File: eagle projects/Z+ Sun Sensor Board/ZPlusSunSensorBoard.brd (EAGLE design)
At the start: 78 x 78 mm, 53 parts, among them U2 ADS7841E_2K5, U4 LM20BIM7X_NOPB, U6 TLV9051IDCKR, U8 TLV9051IDCKR, U9 TLV9051IDCKR

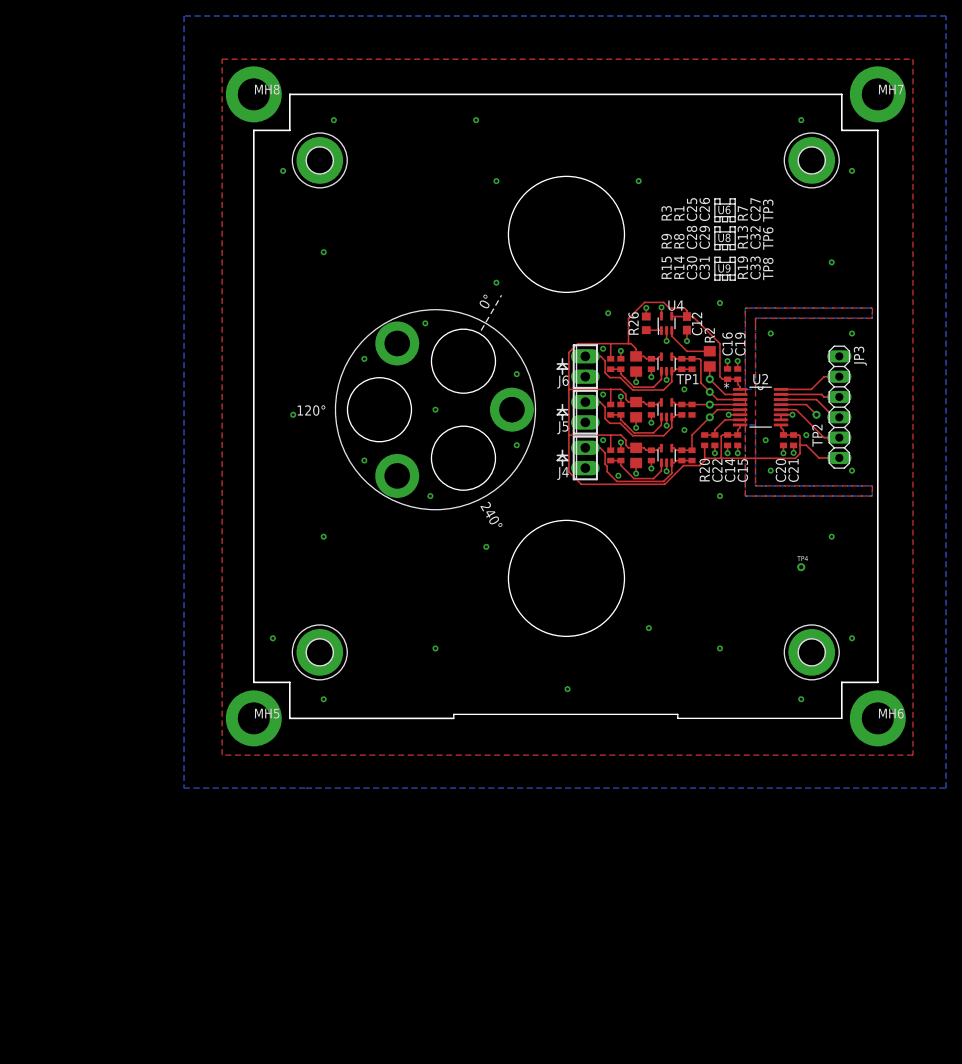
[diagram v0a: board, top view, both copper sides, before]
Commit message: updates to Z+ sun sense board for 3d models
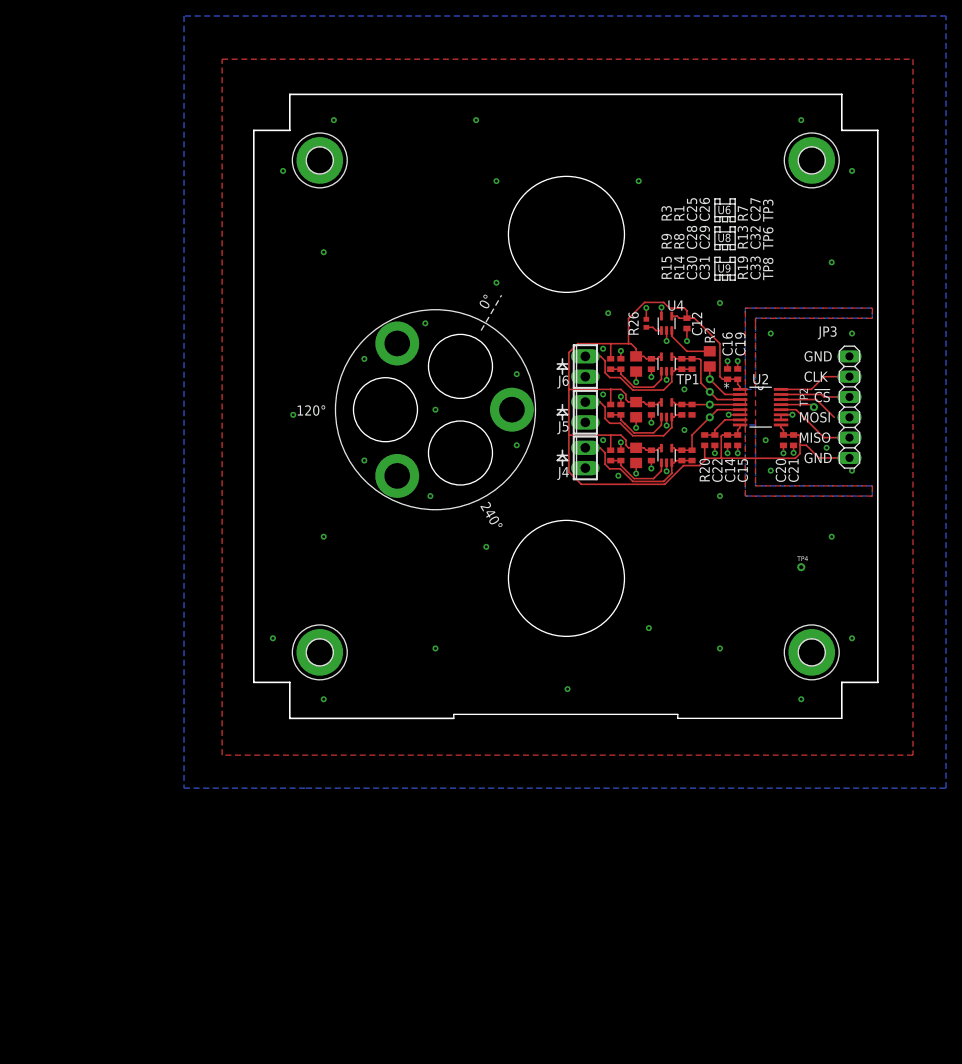
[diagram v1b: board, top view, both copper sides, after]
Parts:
- removed MH5, MH6, MH7, MH8: MTGP700H400, my_library:MTGP700H400
- C12: device rcl:C0603 -> rcl:C0402
- C27, C32, C33: value 0.015u -> 0.022u
- R13, R19, R7: value 5.6k -> 3.74k
- R26: device rcl:R0603 -> rcl:R0402
- moved JP3 1.27 mm to (81.0, 45.4)
- moved TP2 1.00 mm to (76.5, 45.4)
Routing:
- net +3V3: track 138.2 -> 139.8 mm
- net UCB0_SPI_MISO: track 8.74 -> 10.0 mm
- net UCB0_SPI_CLK: track 7.95 -> 9.22 mm
- net !CS!_SUN_Z+: track 7.42 -> 8.69 mm
- net N$2: track 4.96 -> 4.25 mm
- net GND: track 28.2 -> 28.8 mm
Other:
- board text added: "!CS"
- board text added: "CLK"
- board text added: "GND"
- board text added: "MISO"
- board text added: "MOSI"
- board text added: "Z+ SUN SENSE BOARD - Rev A"
- board text removed: "Z+ SUN SENSOR BOARD - Rev A"

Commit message: Finalized sun sense board
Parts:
- added DRILEGEND: (no value), drilegend:DRILEGEND
- H1, H2, H3, H4: value MOUNT-PAD-ROUND3.2 -> MOUNT-PAD-ROUND; device holes:3,2-PAD -> my_library:PC104
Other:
- outline, holes or cut-outs redrawn
- board text added: "+3V3"
- board text added: "01-16"
- board text added: "01-20"
- board text added: "LAYER-STACK"

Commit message: Minor gerber updates to copper
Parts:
- JP3: device pinhead:1X06 -> my_library:1X06
- moved R2 0.32 mm to (63.5, 51.8)
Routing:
- net GND: track 28.8 -> 26.7 mm, vias 69 -> 70
- net UCB0_SPI_MOSI: track 7.58 -> 9.48 mm
- net N$8: track 16.5 -> 17.8 mm

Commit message: bfwebfibc
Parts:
- added R4: 5.1M, resistor:R0402
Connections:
- net GND: now also R4.1
- net N$2: now also R4.2
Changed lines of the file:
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@@
 </element>
 <element name="DRILEGEND" library="drilegend" package="DRILEGEND" value="" x="-4.57708125" y="-7.75208125" smashed="yes"/>
+<element name="R4" library="resistor" library_urn="urn:adsk.eagle:library:348" package="R0402" package3d_urn="urn:adsk.eagle:package:26058/2" value="5.1M" x="-22.225" y="-34.29" smashed="yes">
+<attribute name="NAME" x="-22.86" y="-33.655" size="1.27" layer="25"/>
+<attribute name="VALUE" x="-22.86" y="-36.195" size="1.27" layer="27"/>
+</element>
 </elements>
 <signals>
@@
 </polygon>
 <via x="65.7225" y="43.18" extent="1-16" drill="0.35"/>
+<contactref element="R4" pad="1"/>
+<wire x1="74.93" y1="81.28" x2="81.28" y2="74.93" width="0" layer="19" extent="1-1"/>
+<wire x1="78.74" y1="63.5" x2="81.28" y2="74.93" width="0" layer="19" extent="1-1"/>
+<wire x1="81.28" y1="54.61" x2="78.74" y2="63.5" width="0" layer="19" extent="1-1"/>
+<wire x1="80.9625" y1="51.7525" x2="81.28" y2="54.61" width="0" layer="19" extent="1-1"/>
+<wire x1="71.12" y1="54.61" x2="81.28" y2="54.61" width="0" layer="19" extent="1-1"/>
+<wire x1="66.04" y1="55.88" x2="71.12" y2="54.61" width="0" layer="19" extent="1-1"/>
+<wire x1="65.7225" y1="51.1606" x2="66.04" y2="55.88" width="0" layer="19" extent="1-1"/>
+<wire x1="66.9925" y1="51.1606" x2="65.7225" y2="51.1606" width="0" layer="19" extent="1-1"/>
+<wire x1="60.6425" y1="55.23" x2="66.04" y2="55.88" width="0" layer="19" extent="1-1"/>
+<wire x1="58.1025" y1="53.665659375" x2="60.6425" y2="53.6575" width="0" layer="19" extent="1-1"/>
+<wire x1="57.4525" y1="56.78" x2="58.1025" y2="54.98" width="0" layer="19" extent="1-1"/>
+<wire x1="55.5625" y1="57.8106" x2="57.4675" y2="57.8656" width="0" layer="19" extent="1-1"/>
+<wire x1="58.1025" y1="49.89" x2="58.1025" y2="53.665659375" width="0" layer="19" extent="1-1"/>
+<wire x1="56.1975" y1="50.15" x2="58.1025" y2="49.89" width="0" layer="19" extent="1-1"/>
+<wire x1="54.2925" y1="49.85" x2="56.1975" y2="50.15" width="0" layer="19" extent="1-1"/>
+<wire x1="52.3875" y1="51.45" x2="54.2925" y2="49.85" width="0" layer="19" extent="1-1"/>
+<wire x1="50.165" y1="52.705" x2="52.3875" y2="52.4306" width="0" layer="19" extent="1-1"/>
+<wire x1="60.325" y1="47.625" x2="58.1025" y2="48.8144" width="0" layer="19" extent="1-1"/>
+<wire x1="52.3875" y1="46.7156" x2="54.2925" y2="48.5344" width="0" layer="19" extent="1-1"/>
+<wire x1="50.165" y1="46.99" x2="52.3875" y2="46.7156" width="0" layer="19" extent="1-1"/>
+<wire x1="54.2925" y1="44.135" x2="52.3875" y2="45.735" width="0" layer="19" extent="1-1"/>
+<wire x1="56.1975" y1="44.435" x2="54.2925" y2="44.135" width="0" layer="19" extent="1-1"/>
+<wire x1="58.1025" y1="44.175" x2="56.1975" y2="44.435" width="0" layer="19" extent="1-1"/>
+<wire x1="60.325" y1="42.545" x2="58.1025" y2="43.0994" width="0" layer="19" extent="1-1"/>
+<wire x1="52.3875" y1="41.0006" x2="54.2925" y2="42.8194" width="0" layer="19" extent="1-1"/>
+<wire x1="50.165" y1="41.275" x2="52.3875" y2="41.0006" width="0" layer="19" extent="1-1"/>
+<wire x1="54.2925" y1="38.42" x2="52.3875" y2="40.02" width="0" layer="19" extent="1-1"/>
+<wire x1="56.1975" y1="38.72" x2="54.2925" y2="38.42" width="0" layer="19" extent="1-1"/>
+<wire x1="58.1025" y1="38.46" x2="56.1975" y2="38.72" width="0" layer="19" extent="1-1"/>
+<wire x1="52.07" y1="36.83" x2="54.2925" y2="37.1044" width="0" layer="19" extent="1-1"/>
+<wire x1="47.9425" y1="49.2125" x2="50.165" y2="46.99" width="0" layer="19" extent="1-1"/>
+<wire x1="47.9425" y1="43.4975" x2="50.165" y2="41.275" width="0" layer="19" extent="1-1"/>
+<wire x1="47.9425" y1="37.7825" x2="50.165" y2="41.275" width="0" layer="19" extent="1-1"/>
+<wire x1="64.135" y1="40.625" x2="60.325" y2="42.545" width="0" layer="19" extent="1-1"/>
+<wire x1="65.7225" y1="39.6444" x2="64.135" y2="39.6444" width="0" layer="19" extent="1-1"/>
+<wire x1="66.9925" y1="40.625" x2="65.7225" y2="40.625" width="0" layer="19" extent="1-1"/>
+<wire x1="65.7225" y1="43.18" x2="65.7225" y2="40.625" width="0" layer="19" extent="1-1"/>
+<wire x1="65.865" y1="44.45" x2="65.7225" y2="43.18" width="0" layer="19" extent="1-1"/>
+<wire x1="70.485" y1="41.275" x2="66.9925" y2="40.625" width="0" layer="19" extent="1-1"/>
+<wire x1="72.7075" y1="40.625" x2="70.485" y2="41.275" width="0" layer="19" extent="1-1"/>
+<wire x1="73.9775" y1="40.625" x2="72.7075" y2="40.625" width="0" layer="19" extent="1-1"/>
+<wire x1="71.12" y1="37.465" x2="72.7075" y2="39.6444" width="0" layer="19" extent="1-1"/>
+<wire x1="72.4027" y1="43.815" x2="70.485" y2="41.275" width="0" layer="19" extent="1-1"/>
+<wire x1="72.4027" y1="44.45" x2="72.4027" y2="43.815" width="0" layer="19" extent="1-1"/>
+<wire x1="73.835" y1="44.45" x2="72.4027" y2="44.45" width="0" layer="19" extent="1-1"/>
+<wire x1="78.105" y1="40.3225" x2="73.9775" y2="40.625" width="0" layer="19" extent="1-1"/>
+<wire x1="81.28" y1="37.465" x2="78.105" y2="40.3225" width="0" layer="19" extent="1-1"/>
+<wire x1="50.8" y1="57.15" x2="50.165" y2="52.705" width="0" layer="19" extent="1-1"/>
+<wire x1="64.77" y1="34.29" x2="64.135" y2="39.6444" width="0" layer="19" extent="1-1"/>
+<wire x1="39.37" y1="49.53" x2="47.9425" y2="49.2125" width="0" layer="19" extent="1-1"/>
+<wire x1="78.74" y1="29.21" x2="81.28" y2="37.465" width="0" layer="19" extent="1-1"/>
+<wire x1="74.93" y1="25.4" x2="78.74" y2="29.21" width="0" layer="19" extent="1-1"/>
+<wire x1="39.37" y1="40.64" x2="39.37" y2="49.53" width="0" layer="19" extent="1-1"/>
+<wire x1="81.28" y1="16.51" x2="74.93" y2="25.4" width="0" layer="19" extent="1-1"/>
+<wire x1="74.93" y1="8.89" x2="81.28" y2="16.51" width="0" layer="19" extent="1-1"/>
+<wire x1="29.21" y1="45.085" x2="39.37" y2="49.53" width="0" layer="19" extent="1-1"/>
+<wire x1="28.575" y1="34.29" x2="29.21" y2="45.085" width="0" layer="19" extent="1-1"/>
+<wire x1="20.32" y1="38.735" x2="28.575" y2="34.29" width="0" layer="19" extent="1-1"/>
+<wire x1="35.56" y1="27.94" x2="28.575" y2="34.29" width="0" layer="19" extent="1-1"/>
+<wire x1="11.43" y1="44.45" x2="20.32" y2="38.735" width="0" layer="19" extent="1-1"/>
+<wire x1="15.24" y1="29.21" x2="20.32" y2="38.735" width="0" layer="19" extent="1-1"/>
+<wire x1="27.94" y1="55.88" x2="29.21" y2="45.085" width="0" layer="19" extent="1-1"/>
+<wire x1="20.32" y1="51.435" x2="27.94" y2="55.88" width="0" layer="19" extent="1-1"/>
+<wire x1="36.83" y1="60.96" x2="27.94" y2="55.88" width="0" layer="19" extent="1-1"/>
+<wire x1="64.77" y1="15.24" x2="74.93" y2="8.89" width="0" layer="19" extent="1-1"/>
+<wire x1="55.88" y1="17.78" x2="64.77" y2="15.24" width="0" layer="19" extent="1-1"/>
+<wire x1="36.83" y1="73.66" x2="36.83" y2="60.96" width="0" layer="19" extent="1-1"/>
+<wire x1="34.29" y1="81.28" x2="36.83" y2="73.66" width="0" layer="19" extent="1-1"/>
+<wire x1="45.72" y1="10.16" x2="55.88" y2="17.78" width="0" layer="19" extent="1-1"/>
+<wire x1="29.21" y1="15.24" x2="35.56" y2="27.94" width="0" layer="19" extent="1-1"/>
+<wire x1="8.89" y1="16.51" x2="15.24" y2="29.21" width="0" layer="19" extent="1-1"/>
+<wire x1="15.24" y1="8.89" x2="8.89" y2="16.51" width="0" layer="19" extent="1-1"/>
+<wire x1="15.24" y1="64.77" x2="20.32" y2="51.435" width="0" layer="19" extent="1-1"/>
+<wire x1="10.16" y1="74.93" x2="15.24" y2="64.77" width="0" layer="19" extent="1-1"/>
+<wire x1="16.51" y1="81.28" x2="10.16" y2="74.93" width="0" layer="19" extent="1-1"/>
+<wire x1="54.61" y1="73.66" x2="55.5625" y2="57.8106" width="0" layer="19" extent="1-1"/>
+<wire x1="-22.875" y1="-34.29" x2="15.24" y2="8.89" width="0" layer="19" extent="1-1"/>
 </signal>
 <signal name="UCB0_SPI_CLK">
@@
 <wire x1="76.5175" y1="45.4025" x2="75.2475" y2="45.4025" width="0.2032" layer="1"/>
 <wire x1="75.2475" y1="45.4025" x2="74.93" y2="45.72" width="0.2032" layer="1"/>
+<contactref element="R4" pad="2"/>
+<wire x1="-21.575" y1="-34.29" x2="72.4027" y2="45.72" width="0" layer="19" extent="1-1"/>
 </signal>
 <signal name="N$4">
